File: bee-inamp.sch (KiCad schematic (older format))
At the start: 15 parts, among them J1 Conn_01x02_Male, J2 Conn_01x02_Male, J3 Conn_01x02_Male, J4 Conn_01x02_Male, J5 Conn_01x02, J6 Conn_01x02, J7 Conn_02x03_Odd_Even, J8 Conn_01x03, J9 Conn_01x02, U1 INA126

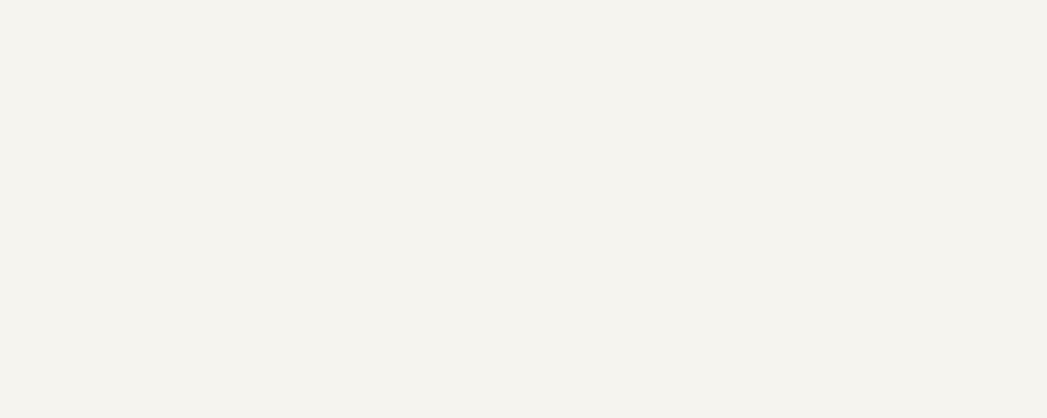
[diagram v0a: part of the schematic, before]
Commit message: Update labels and mounting holes.
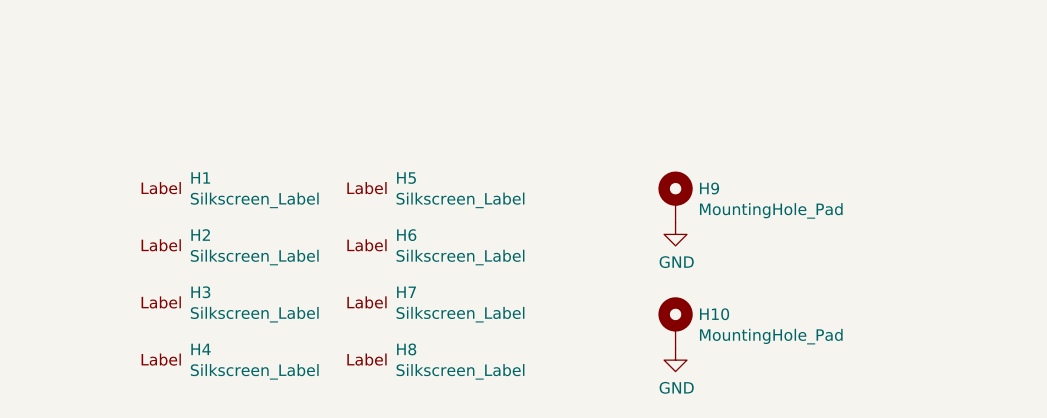
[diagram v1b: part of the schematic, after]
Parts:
- added H1, H2: Silkscreen_Label, Symbol-emt:Text_U_B+_Silkscreen, symbol Mechanical-emt:Silkscreen_Label
- added H10, H9: MountingHole_Pad, MountingHole:MountingHole_3.2mm_M3_ISO7380_Pad, symbol Mechanical:MountingHole_Pad
- added H3, H4: Silkscreen_Label, Symbol-emt:Text_U_B-_Silkscreen, symbol Mechanical-emt:Silkscreen_Label
- added H5, H6: Silkscreen_Label, Symbol-emt:Text_U_B2_Silkscreen, symbol Mechanical-emt:Silkscreen_Label
- added H7, H8: Silkscreen_Label, Symbol-emt:Symbol_GND_Silkscreen, symbol Mechanical-emt:Silkscreen_Label
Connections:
- net GND: now also H10.1, H9.1
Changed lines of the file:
@@
 	0    1    1    0
 $EndComp
+$Comp
+L Mechanical-emt:Silkscreen_Label H1
+U 1 1 5CC837C1
+P 1200 6800
+F 0 "H1" H 1325 6845 50  0000 L CNN
+F 1 "Silkscreen_Label" H 1325 6754 50  0000 L CNN
+F 2 "Symbol-emt:Text_U_B+_Silkscreen" H 1200 6800 50  0001 C CNN
+F 3 "~" H 1200 6800 50  0001 C CNN
+	1    1200 6800
+	1    0    0    -1
+$EndComp
+$Comp
+L Mechanical-emt:Silkscreen_Label H2
+U 1 1 5CC83EDA
+P 1200 7050
+F 0 "H2" H 1325 7095 50  0000 L CNN
+F 1 "Silkscreen_Label" H 1325 7004 50  0000 L CNN
+F 2 "Symbol-emt:Text_U_B+_Silkscreen" H 1200 7050 50  0001 C CNN
+F 3 "~" H 1200 7050 50  0001 C CNN
+	1    1200 7050
+	1    0    0    -1
+$EndComp
+$Comp
+L Mechanical-emt:Silkscreen_Label H3
+U 1 1 5CC84084
+P 1200 7300
+F 0 "H3" H 1325 7345 50  0000 L CNN
+F 1 "Silkscreen_Label" H 1325 7254 50  0000 L CNN
+F 2 "Symbol-emt:Text_U_B-_Silkscreen" H 1200 7300 50  0001 C CNN
+F 3 "~" H 1200 7300 50  0001 C CNN
+	1    1200 7300
+	1    0    0    -1
+$EndComp
+$Comp
+L Mechanical-emt:Silkscreen_Label H4
+U 1 1 5CC843C8
+P 1200 7550
+F 0 "H4" H 1325 7595 50  0000 L CNN
+F 1 "Silkscreen_Label" H 1325 7504 50  0000 L CNN
+F 2 "Symbol-emt:Text_U_B-_Silkscreen" H 1200 7550 50  0001 C CNN
+F 3 "~" H 1200 7550 50  0001 C CNN
+	1    1200 7550
+	1    0    0    -1
+$EndComp
+$Comp
+L Mechanical-emt:Silkscreen_Label H5
+U 1 1 5CC8460D
+P 2100 6800
+F 0 "H5" H 2225 6845 50  0000 L CNN
+F 1 "Silkscreen_Label" H 2225 6754 50  0000 L CNN
+F 2 "Symbol-emt:Text_U_B2_Silkscreen" H 2100 6800 50  0001 C CNN
+F 3 "~" H 2100 6800 50  0001 C CNN
+	1    2100 6800
+	1    0    0    -1
+$EndComp
+$Comp
+L Mechanical-emt:Silkscreen_Label H6
+U 1 1 5CC84A78
+P 2100 7050
+F 0 "H6" H 2225 7095 50  0000 L CNN
+F 1 "Silkscreen_Label" H 2225 7004 50  0000 L CNN
+F 2 "Symbol-emt:Text_U_B2_Silkscreen" H 2100 7050 50  0001 C CNN
+F 3 "~" H 2100 7050 50  0001 C CNN
+	1    2100 7050
+	1    0    0    -1
+$EndComp
+$Comp
+L Mechanical-emt:Silkscreen_Label H7
+U 1 1 5CC84D85
+P 2100 7300
+F 0 "H7" H 2225 7345 50  0000 L CNN
+F 1 "Silkscreen_Label" H 2225 7254 50  0000 L CNN
+F 2 "Symbol-emt:Symbol_GND_Silkscreen" H 2100 7300 50  0001 C CNN
+F 3 "~" H 2100 7300 50  0001 C CNN
+	1    2100 7300
+	1    0    0    -1
+$EndComp
+$Comp
+L Mechanical-emt:Silkscreen_Label H8
+U 1 1 5CC84F20
+P 2100 7550
+F 0 "H8" H 2225 7595 50  0000 L CNN
+F 1 "Silkscreen_Label" H 2225 7504 50  0000 L CNN
+F 2 "Symbol-emt:Symbol_GND_Silkscreen" H 2100 7550 50  0001 C CNN
+F 3 "~" H 2100 7550 50  0001 C CNN
+	1    2100 7550
+	1    0    0    -1
+$EndComp
+$Comp
+L Mechanical:MountingHole_Pad H9
+U 1 1 5CC85962
+P 3450 6850
+F 0 "H9" H 3550 6899 50  0000 L CNN
+F 1 "MountingHole_Pad" H 3550 6808 50  0000 L CNN
+F 2 "MountingHole:MountingHole_3.2mm_M3_ISO7380_Pad" H 3450 6850 50  0001 C CNN
+F 3 "~" H 3450 6850 50  0001 C CNN
+	1    3450 6850
+	1    0    0    -1
+$EndComp
+$Comp
+L Mechanical:MountingHole_Pad H10
+U 1 1 5CC860DE
+P 3450 7400
+F 0 "H10" H 3550 7449 50  0000 L CNN
+F 1 "MountingHole_Pad" H 3550 7358 50  0000 L CNN
+F 2 "MountingHole:MountingHole_3.2mm_M3_ISO7380_Pad" H 3450 7400 50  0001 C CNN
+F 3 "~" H 3450 7400 50  0001 C CNN
+	1    3450 7400
+	1    0    0    -1
+$EndComp
+$Comp
+L power:GND #PWR0108
+U 1 1 5CC872D7
+P 3450 6950
+F 0 "#PWR0108" H 3450 6700 50  0001 C CNN
+F 1 "GND" H 3455 6777 50  0000 C CNN
+F 2 "" H 3450 6950 50  0001 C CNN
+F 3 "" H 3450 6950 50  0001 C CNN
+	1    3450 6950
+	1    0    0    -1
+$EndComp
+$Comp
+L power:GND #PWR0109
+U 1 1 5CC8791F
+P 3450 7500
+F 0 "#PWR0109" H 3450 7250 50  0001 C CNN
+F 1 "GND" H 3455 7327 50  0000 C CNN
+F 2 "" H 3450 7500 50  0001 C CNN
+F 3 "" H 3450 7500 50  0001 C CNN
+	1    3450 7500
+	1    0    0    -1
+$EndComp
 $EndSCHEMATC

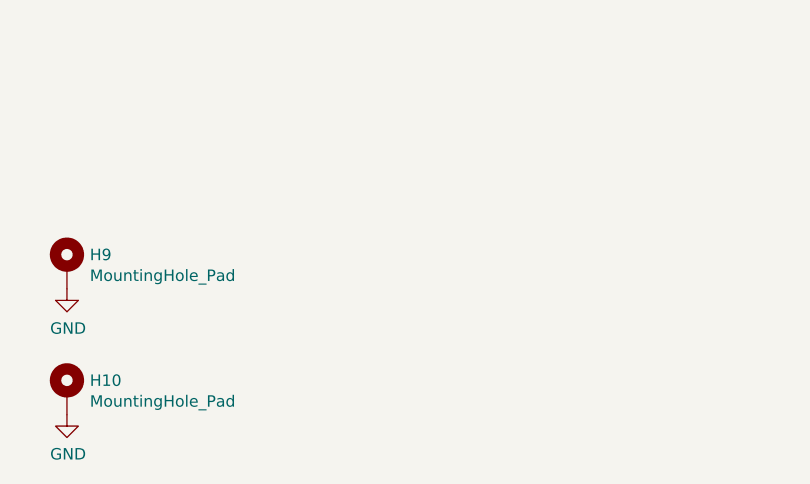
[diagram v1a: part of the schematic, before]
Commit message: Add text and logos.
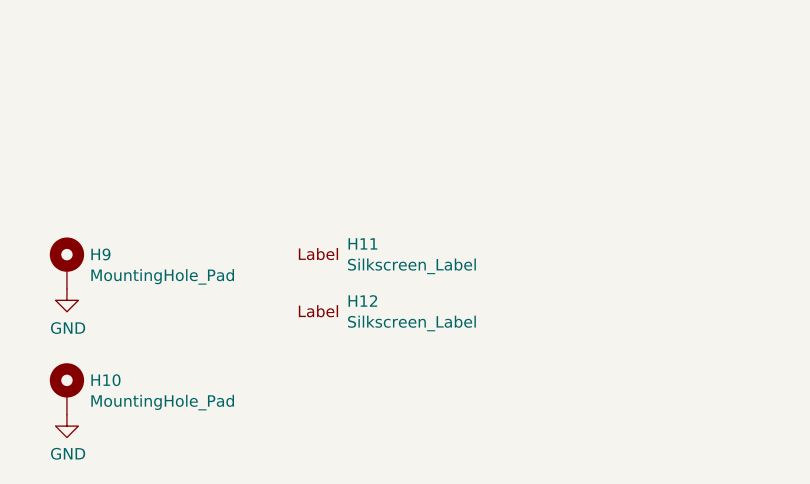
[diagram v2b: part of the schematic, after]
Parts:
- added H11: Silkscreen_Label, Symbol-emt:EMT-Logo_5.1x2.5mm_Silkscreen, symbol Mechanical-emt:Silkscreen_Label
- added H12: Silkscreen_Label, Symbol-emt:BEE-Logo_Silkscreen_small, symbol Mechanical-emt:Silkscreen_Label
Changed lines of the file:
@@
 EESchema Schematic File Version 4
 LIBS:bee-inamp-cache
-EELAYER 29 0
+EELAYER 26 0
 EELAYER END
 $Descr A4 11693 8268
@@
 	1    0    0    -1
 $EndComp
+$Comp
+L Mechanical-emt:Silkscreen_Label H11
+U 1 1 5CCC571C
+P 4550 6800
+F 0 "H11" H 4675 6845 50  0000 L CNN
+F 1 "Silkscreen_Label" H 4675 6754 50  0000 L CNN
+F 2 "Symbol-emt:EMT-Logo_5.1x2.5mm_Silkscreen" H 4550 6800 50  0001 C CNN
+F 3 "~" H 4550 6800 50  0001 C CNN
+	1    4550 6800
+	1    0    0    -1
+$EndComp
+$Comp
+L Mechanical-emt:Silkscreen_Label H12
+U 1 1 5CCC5878
+P 4550 7050
+F 0 "H12" H 4675 7095 50  0000 L CNN
+F 1 "Silkscreen_Label" H 4675 7004 50  0000 L CNN
+F 2 "Symbol-emt:BEE-Logo_Silkscreen_small" H 4550 7050 50  0001 C CNN
+F 3 "~" H 4550 7050 50  0001 C CNN
+	1    4550 7050
+	1    0    0    -1
+$EndComp

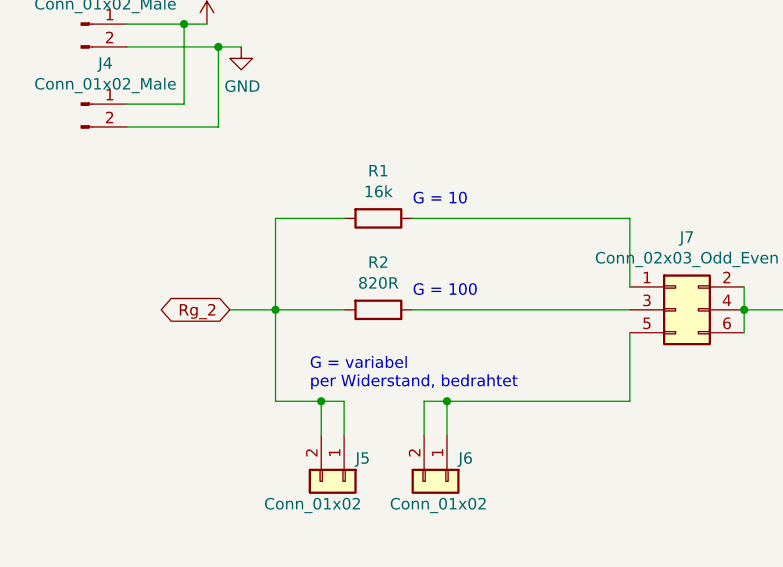
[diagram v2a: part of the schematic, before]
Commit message: Add part numbers.
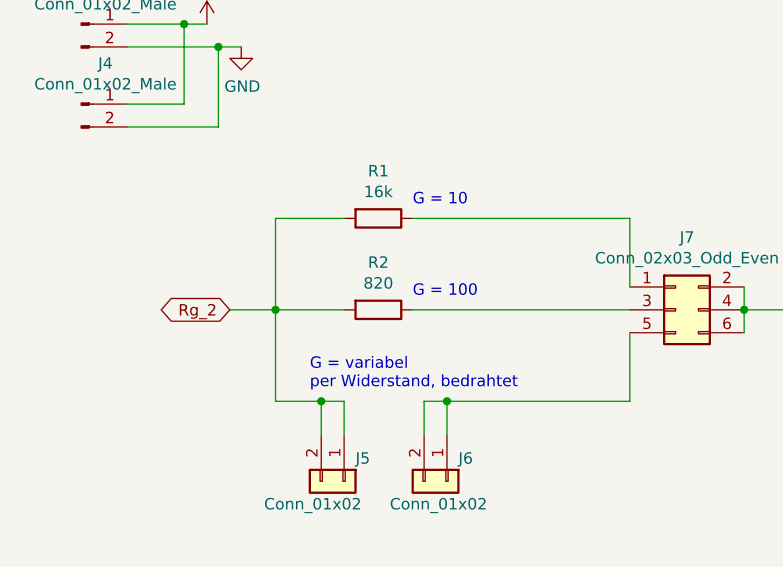
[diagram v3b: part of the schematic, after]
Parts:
- C1, C2: Reichelt Part No (none) -> X7R-G0805 100N; order number KEM X7R0805 100N -> (none)
- J1, J2, J3, J4, J9: Reichelt Part No (none) -> RND 205-00623
- J5, J6: Reichelt Part No (none) -> MPE 006-1-002
- J7: Reichelt Part No (none) -> RND 205-00634
- J8: Reichelt Part No (none) -> RND 205-00624
- R1: Reichelt Part No (none) -> RND 0805 1 16K
- R2: value 820R -> 820; Reichelt Part No (none) -> RND 0805 1 820
- U1: Reichelt Part No (none) -> INA 126 UA/2K5; order number INA 126 UA/2K5 -> (none)
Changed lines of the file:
@@
 F 2 "Connector_PinHeader_2.54mm:PinHeader_1x02_P2.54mm_Vertical" H 850 1300 50  0001 C CNN
 F 3 "~" H 850 1300 50  0001 C CNN
+F 4 "RND 205-00623" H 850 1300 50  0001 C CNN "Reichelt Part No"
 	1    850  1300
 	1    0    0    -1
@@
 F 2 "Connector_PinHeader_2.54mm:PinHeader_1x02_P2.54mm_Vertical" H 850 950 50  0001 C CNN
 F 3 "~" H 850 950 50  0001 C CNN
+F 4 "RND 205-00623" H 850 950 50  0001 C CNN "Reichelt Part No"
 	1    850  950
 	1    0    0    -1
@@
 F 2 "Connector_PinHeader_2.54mm:PinHeader_1x02_P2.54mm_Vertical" H 850 2150 50  0001 C CNN
 F 3 "~" H 850 2150 50  0001 C CNN
+F 4 "RND 205-00623" H 850 2150 50  0001 C CNN "Reichelt Part No"
 	1    850  2150
 	1    0    0    -1
@@
 F 2 "Connector_PinHeader_2.54mm:PinHeader_1x02_P2.54mm_Vertical" H 850 1800 50  0001 C CNN
 F 3 "~" H 850 1800 50  0001 C CNN
+F 4 "RND 205-00623" H 850 1800 50  0001 C CNN "Reichelt Part No"
 	1    850  1800
 	1    0    0    -1
@@
 F 2 "Resistor_SMD:R_0805_2012Metric_Pad1.15x1.40mm_HandSolder" V 2080 2650 50  0001 C CNN
 F 3 "~" H 2150 2650 50  0001 C CNN
+F 4 "RND 0805 1 16K" H 2150 2650 50  0001 C CNN "Reichelt Part No"
 	1    2150 2650
 	0    1    1    0
@@
 P 2150 3050
 F 0 "R2" V 1943 3050 50  0000 C CNN
-F 1 "820R" V 2034 3050 50  0000 C CNN
+F 1 "820" V 2034 3050 50  0000 C CNN
 F 2 "Resistor_SMD:R_0805_2012Metric_Pad1.15x1.40mm_HandSolder" V 2080 3050 50  0001 C CNN
 F 3 "~" H 2150 3050 50  0001 C CNN
+F 4 "RND 0805 1 820" H 2150 3050 50  0001 C CNN "Reichelt Part No"
 	1    2150 3050
 	0    1    1    0
@@
 F 1 "0.1µF" V 5839 2550 50  0000 C CNN
 F 2 "Capacitor_SMD:C_0805_2012Metric_Pad1.15x1.40mm_HandSolder" H 6038 2400 50  0001 C CNN
-F 3 "https://www.reichelt.de/index.html?ACTION=7&LA=3&OPEN=0&INDEX=0&FILENAME=B300%252FKEM_C0XXX_X7R_DB-EN.pdf" H 6000 2550 50  0001 C CNN
-F 4 "KEM X7R0805 100N" H 6000 2550 50  0001 C CNN "order number"
+F 3 "~" H 6000 2550 50  0001 C CNN
+F 4 "X7R-G0805 100N" H 6000 2550 50  0001 C CNN "Reichelt Part No"
 	1    6000 2550
 	0    1    1    0
@@
 F 1 "0.1µF" V 5839 3650 50  0000 C CNN
 F 2 "Capacitor_SMD:C_0805_2012Metric_Pad1.15x1.40mm_HandSolder" H 6038 3500 50  0001 C CNN
-F 3 "https://www.reichelt.de/index.html?ACTION=7&LA=3&OPEN=0&INDEX=0&FILENAME=B300%252FKEM_C0XXX_X7R_DB-EN.pdf" H 6000 3650 50  0001 C CNN
-F 4 "KEM X7R0805 100N" H 6000 3650 50  0001 C CNN "order number"
+F 3 "~" H 6000 3650 50  0001 C CNN
+F 4 "X7R-G0805 100N" H 6000 3650 50  0001 C CNN "Reichelt Part No"
 	1    6000 3650
 	0    1    1    0
@@
 F 2 "Package_SO:SO-8_5.3x6.2mm_P1.27mm" H 6400 3100 50  0001 C CNN
 F 3 "http://www.ti.com/lit/ds/symlink/ina128.pdf" H 6400 3100 50  0001 C CNN
-F 4 "INA 126 UA/2K5" H 6300 3100 50  0001 C CNN "order number"
+F 4 "INA 126 UA/2K5" H 6300 3100 50  0001 C CNN "Reichelt Part No"
 	1    6300 3100
 	1    0    0    -1
@@
 F 2 "Connector_PinHeader_2.54mm:PinHeader_2x03_P2.54mm_Vertical_SMD" H 3450 3050 50  0001 C CNN
 F 3 "~" H 3450 3050 50  0001 C CNN
+F 4 "RND 205-00634" H 3450 3050 50  0001 C CNN "Reichelt Part No"
 	1    3450 3050
 	1    0    0    -1
@@
 F 2 "Connector_PinHeader_2.54mm:PinHeader_1x03_P2.54mm_Vertical" H 5000 3100 50  0001 C CNN
 F 3 "~" H 5000 3100 50  0001 C CNN
+F 4 "RND 205-00624" H 5000 3100 50  0001 C CNN "Reichelt Part No"
 	1    5000 3100
 	-1   0    0    -1
@@
 F 2 "Connector_PinHeader_2.54mm:PinHeader_1x02_P2.54mm_Vertical" H 7600 3100 50  0001 C CNN
 F 3 "~" H 7600 3100 50  0001 C CNN
+F 4 "RND 205-00623" H 7600 3100 50  0001 C CNN "Reichelt Part No"
 	1    7600 3100
 	1    0    0    -1
@@
 F 2 "Connector_PinSocket_2.54mm:PinSocket_1x02_P2.54mm_Vertical" H 2000 3800 50  0001 C CNN
 F 3 "~" H 2000 3800 50  0001 C CNN
+F 4 "MPE 006-1-002" H 2000 3800 50  0001 C CNN "Reichelt Part No"
 	1    2000 3800
 	0    1    1    0
@@
 F 2 "Connector_PinSocket_2.54mm:PinSocket_1x02_P2.54mm_Vertical" H 2450 3800 50  0001 C CNN
 F 3 "~" H 2450 3800 50  0001 C CNN
+F 4 "MPE 006-1-002" H 2450 3800 50  0001 C CNN "Reichelt Part No"
 	1    2450 3800
 	0    1    1    0

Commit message: Fix order number (THT->SMD).
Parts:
- J7: Reichelt Part No RND 205-00634 -> SL 2X10G SMD2,54
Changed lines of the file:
@@
 F 2 "Connector_PinHeader_2.54mm:PinHeader_2x03_P2.54mm_Vertical_SMD" H 3450 3050 50  0001 C CNN
 F 3 "~" H 3450 3050 50  0001 C CNN
-F 4 "RND 205-00634" H 3450 3050 50  0001 C CNN "Reichelt Part No"
+F 4 "SL 2X10G SMD2,54" H 3450 3050 50  0001 C CNN "Reichelt Part No"
 	1    3450 3050
 	1    0    0    -1

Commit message: Replace SO package by SOIC. Fixes #1.
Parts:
- U1: footprint Package_SO:SO-8_5.3x6.2mm_P1.27mm -> Package_SO:SOIC-8_3.9x4.9mm_P1.27mm
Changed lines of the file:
@@
 F 0 "U1" H 6744 3146 50  0000 L CNN
 F 1 "INA126" H 6744 3055 50  0000 L CNN
-F 2 "Package_SO:SO-8_5.3x6.2mm_P1.27mm" H 6400 3100 50  0001 C CNN
+F 2 "Package_SO:SOIC-8_3.9x4.9mm_P1.27mm" H 6400 3100 50  0001 C CNN
 F 3 "http://www.ti.com/lit/ds/symlink/ina128.pdf" H 6400 3100 50  0001 C CNN
 F 4 "INA 126 UA/2K5" H 6300 3100 50  0001 C CNN "Reichelt Part No"

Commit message: Relabel as bee specific.
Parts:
- H1, H2: footprint Symbol-emt:Text_U_B+_Silkscreen -> Symbol-bee:Text_U_B+_Silkscreen; symbol Mechanical-emt:Silkscreen_Label -> Mechanical-bee:Silkscreen_Label
- H11: footprint Symbol-emt:EMT-Logo_5.1x2.5mm_Silkscreen -> Symbol-bee:EMT-Logo_5.1x2.5mm_Silkscreen; symbol Mechanical-emt:Silkscreen_Label -> Mechanical-bee:Silkscreen_Label
- H12: footprint Symbol-emt:BEE-Logo_Silkscreen_small -> Symbol-bee:BEE-Logo_Silkscreen_small; symbol Mechanical-emt:Silkscreen_Label -> Mechanical-bee:Silkscreen_Label
- H3, H4: footprint Symbol-emt:Text_U_B-_Silkscreen -> Symbol-bee:Text_U_B-_Silkscreen; symbol Mechanical-emt:Silkscreen_Label -> Mechanical-bee:Silkscreen_Label
- H5, H6: footprint Symbol-emt:Text_U_B2_Silkscreen -> Symbol-bee:Text_U_B2_Silkscreen; symbol Mechanical-emt:Silkscreen_Label -> Mechanical-bee:Silkscreen_Label
- H7, H8: footprint Symbol-emt:Symbol_GND_Silkscreen -> Symbol-bee:Symbol_GND_Silkscreen; symbol Mechanical-emt:Silkscreen_Label -> Mechanical-bee:Silkscreen_Label
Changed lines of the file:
@@
 $EndComp
 $Comp
-L Mechanical-emt:Silkscreen_Label H1
+L Mechanical-bee:Silkscreen_Label H1
 U 1 1 5CC837C1
 P 1200 6800
 F 0 "H1" H 1325 6845 50  0000 L CNN
 F 1 "Silkscreen_Label" H 1325 6754 50  0000 L CNN
-F 2 "Symbol-emt:Text_U_B+_Silkscreen" H 1200 6800 50  0001 C CNN
+F 2 "Symbol-bee:Text_U_B+_Silkscreen" H 1200 6800 50  0001 C CNN
 F 3 "~" H 1200 6800 50  0001 C CNN
 	1    1200 6800
@@
 $EndComp
 $Comp
-L Mechanical-emt:Silkscreen_Label H2
+L Mechanical-bee:Silkscreen_Label H2
 U 1 1 5CC83EDA
 P 1200 7050
 F 0 "H2" H 1325 7095 50  0000 L CNN
 F 1 "Silkscreen_Label" H 1325 7004 50  0000 L CNN
-F 2 "Symbol-emt:Text_U_B+_Silkscreen" H 1200 7050 50  0001 C CNN
+F 2 "Symbol-bee:Text_U_B+_Silkscreen" H 1200 7050 50  0001 C CNN
 F 3 "~" H 1200 7050 50  0001 C CNN
 	1    1200 7050
@@
 $EndComp
 $Comp
-L Mechanical-emt:Silkscreen_Label H3
+L Mechanical-bee:Silkscreen_Label H3
 U 1 1 5CC84084
 P 1200 7300
 F 0 "H3" H 1325 7345 50  0000 L CNN
 F 1 "Silkscreen_Label" H 1325 7254 50  0000 L CNN
-F 2 "Symbol-emt:Text_U_B-_Silkscreen" H 1200 7300 50  0001 C CNN
+F 2 "Symbol-bee:Text_U_B-_Silkscreen" H 1200 7300 50  0001 C CNN
 F 3 "~" H 1200 7300 50  0001 C CNN
 	1    1200 7300
@@
 $EndComp
 $Comp
-L Mechanical-emt:Silkscreen_Label H4
+L Mechanical-bee:Silkscreen_Label H4
 U 1 1 5CC843C8
 P 1200 7550
 F 0 "H4" H 1325 7595 50  0000 L CNN
 F 1 "Silkscreen_Label" H 1325 7504 50  0000 L CNN
-F 2 "Symbol-emt:Text_U_B-_Silkscreen" H 1200 7550 50  0001 C CNN
+F 2 "Symbol-bee:Text_U_B-_Silkscreen" H 1200 7550 50  0001 C CNN
 F 3 "~" H 1200 7550 50  0001 C CNN
 	1    1200 7550
@@
 $EndComp
 $Comp
-L Mechanical-emt:Silkscreen_Label H5
+L Mechanical-bee:Silkscreen_Label H5
 U 1 1 5CC8460D
 P 2100 6800
 F 0 "H5" H 2225 6845 50  0000 L CNN
 F 1 "Silkscreen_Label" H 2225 6754 50  0000 L CNN
-F 2 "Symbol-emt:Text_U_B2_Silkscreen" H 2100 6800 50  0001 C CNN
+F 2 "Symbol-bee:Text_U_B2_Silkscreen" H 2100 6800 50  0001 C CNN
 F 3 "~" H 2100 6800 50  0001 C CNN
 	1    2100 6800
@@
 $EndComp
 $Comp
-L Mechanical-emt:Silkscreen_Label H6
+L Mechanical-bee:Silkscreen_Label H6
 U 1 1 5CC84A78
 P 2100 7050
 F 0 "H6" H 2225 7095 50  0000 L CNN
 F 1 "Silkscreen_Label" H 2225 7004 50  0000 L CNN
-F 2 "Symbol-emt:Text_U_B2_Silkscreen" H 2100 7050 50  0001 C CNN
+F 2 "Symbol-bee:Text_U_B2_Silkscreen" H 2100 7050 50  0001 C CNN
 F 3 "~" H 2100 7050 50  0001 C CNN
 	1    2100 7050
@@
 $EndComp
 $Comp
-L Mechanical-emt:Silkscreen_Label H7
+L Mechanical-bee:Silkscreen_Label H7
 U 1 1 5CC84D85
 P 2100 7300
 F 0 "H7" H 2225 7345 50  0000 L CNN
 F 1 "Silkscreen_Label" H 2225 7254 50  0000 L CNN
-F 2 "Symbol-emt:Symbol_GND_Silkscreen" H 2100 7300 50  0001 C CNN
+F 2 "Symbol-bee:Symbol_GND_Silkscreen" H 2100 7300 50  0001 C CNN
 F 3 "~" H 2100 7300 50  0001 C CNN
 	1    2100 7300
@@
 $EndComp
 $Comp
-L Mechanical-emt:Silkscreen_Label H8
+L Mechanical-bee:Silkscreen_Label H8
 U 1 1 5CC84F20
 P 2100 7550
 F 0 "H8" H 2225 7595 50  0000 L CNN
 F 1 "Silkscreen_Label" H 2225 7504 50  0000 L CNN
-F 2 "Symbol-emt:Symbol_GND_Silkscreen" H 2100 7550 50  0001 C CNN
+F 2 "Symbol-bee:Symbol_GND_Silkscreen" H 2100 7550 50  0001 C CNN
 F 3 "~" H 2100 7550 50  0001 C CNN
 	1    2100 7550
@@
 $EndComp
 $Comp
-L Mechanical-emt:Silkscreen_Label H11
+L Mechanical-bee:Silkscreen_Label H11
 U 1 1 5CCC571C
 P 4550 6800
 F 0 "H11" H 4675 6845 50  0000 L CNN
 F 1 "Silkscreen_Label" H 4675 6754 50  0000 L CNN
-F 2 "Symbol-emt:EMT-Logo_5.1x2.5mm_Silkscreen" H 4550 6800 50  0001 C CNN
+F 2 "Symbol-bee:EMT-Logo_5.1x2.5mm_Silkscreen" H 4550 6800 50  0001 C CNN
 F 3 "~" H 4550 6800 50  0001 C CNN
 	1    4550 6800
@@
 $EndComp
 $Comp
-L Mechanical-emt:Silkscreen_Label H12
+L Mechanical-bee:Silkscreen_Label H12
 U 1 1 5CCC5878
 P 4550 7050
 F 0 "H12" H 4675 7095 50  0000 L CNN
 F 1 "Silkscreen_Label" H 4675 7004 50  0000 L CNN
-F 2 "Symbol-emt:BEE-Logo_Silkscreen_small" H 4550 7050 50  0001 C CNN
+F 2 "Symbol-bee:BEE-Logo_Silkscreen_small" H 4550 7050 50  0001 C CNN
 F 3 "~" H 4550 7050 50  0001 C CNN
 	1    4550 7050
